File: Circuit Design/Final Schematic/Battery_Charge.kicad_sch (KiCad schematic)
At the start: 9 parts

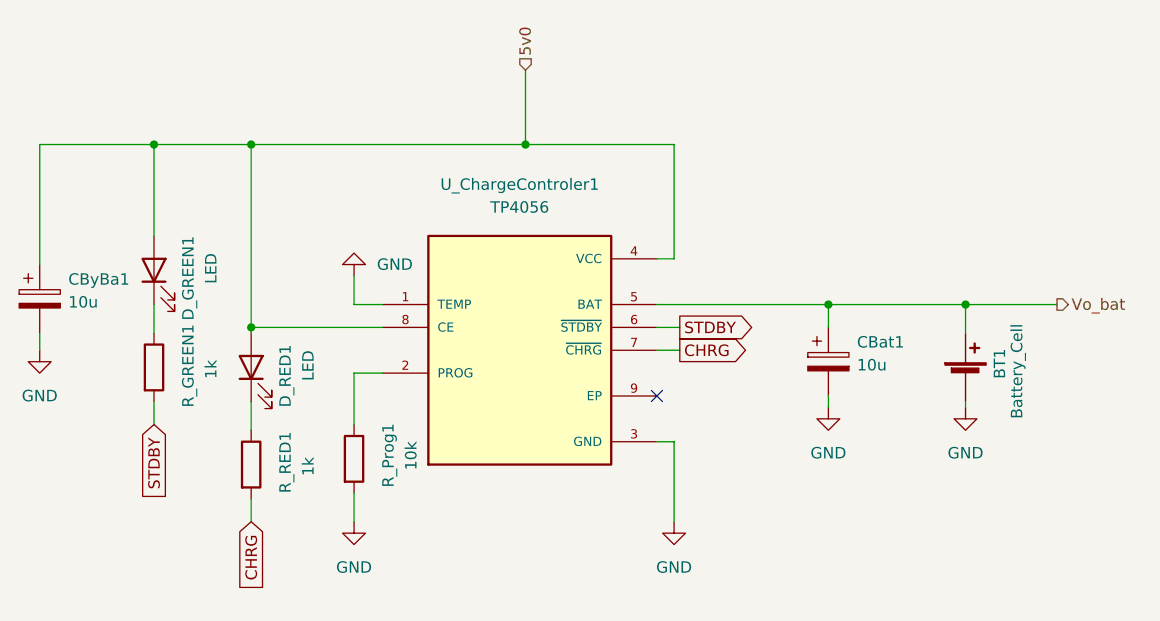
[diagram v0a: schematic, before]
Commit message: Ruteo de PCB
Se agregó el ruteo de la PCB verificando las conexiones
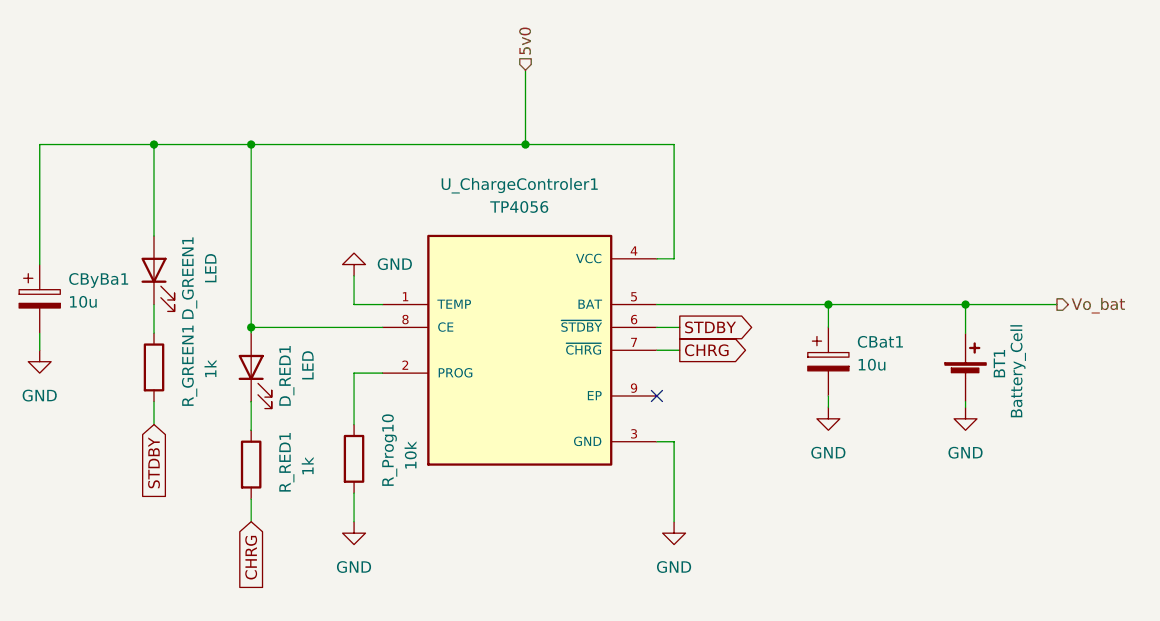
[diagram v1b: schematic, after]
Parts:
- renumbered R_Prog1 to R_Prog10
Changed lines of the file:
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@@
   (symbol (lib_id "Device:R") (at 128.27 114.3 0) (unit 1)
     (in_bom yes) (on_board yes)
-    (property "Reference" "R_Prog1" (id 0) (at 132.08 117.475 90)
+    (property "Reference" "R_Prog10" (id 0) (at 132.08 117.475 90)
       (effects (font (size 1.27 1.27)) (justify left))
     )
